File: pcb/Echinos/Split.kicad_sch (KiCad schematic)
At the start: 43 parts, among them J1 Conn_01x06_Socket, J2 Conn_01x06_Socket, J3 Conn_01x06_Socket, J5 Conn_01x05_Socket, J6 USB_B_Micro, J7 Conn_01x04_Socket, J8 USB_C_Receptacle_USB2.0, U2 USBLC6-2P6, U3 XC6210B332MR-G, U7 USBLC6-2P6, U8 74LVC1T45

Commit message: [PCB] - Save last state with on board RP2040.   - Create right side and route all components   - Component still on the bottom side to be able to merge both side for manufacturing
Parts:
- renumbered C3 to C222, C1 to C223, C2 to C224, D3 to D231, D1 to D232, F2 to F200, F3 to F201, FB1 to FB200, H1 to H200, H2 to H201, H5 to H202, H3 to H203, H4 to H204, H6 to H205, J6 to J200, J7 to J201, J4 to J202, J1 to J203, J2 to J204, J3 to J205, J8 to J206, J5 to J207, JP0 to JP200, JP13 to JP201, JP14 to JP202, JP15 to JP203, JP16 to JP204, JP11 to JP205, JP12 to JP206, JP205 to JP207, R13 to R206, R14 to R207, R15 to R208, R16 to R209, R7 to R210, R8 to R211, R9 to R212, R12 to R213, R1 to R214, U7 to U202, U8 to U203, U2 to U204, U3 to U205
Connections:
- net GND: now also J201.4 (Pin_4); no longer J201.1 (Pin_1)
- net P_RX: now also J201.3 (Pin_3); no longer J201.2 (Pin_2)
- net P_TX: now also J201.2 (Pin_2); no longer J201.3 (Pin_3)
- net VBUS_split: now also J201.1 (Pin_1); no longer J201.4 (Pin_4)
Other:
- sheet Backlight: file LED_left.kicad_sch -> LED.kicad_sch
- sheet Matrix: file Keyboard_Matrix.kicad_sch -> Matrix.kicad_sch
- title: Echinos -> Echinos Left
- moved on the sheet: C222, C223, C224, D231, D232, F200, F201, FB200, H200, H201, H202, H203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

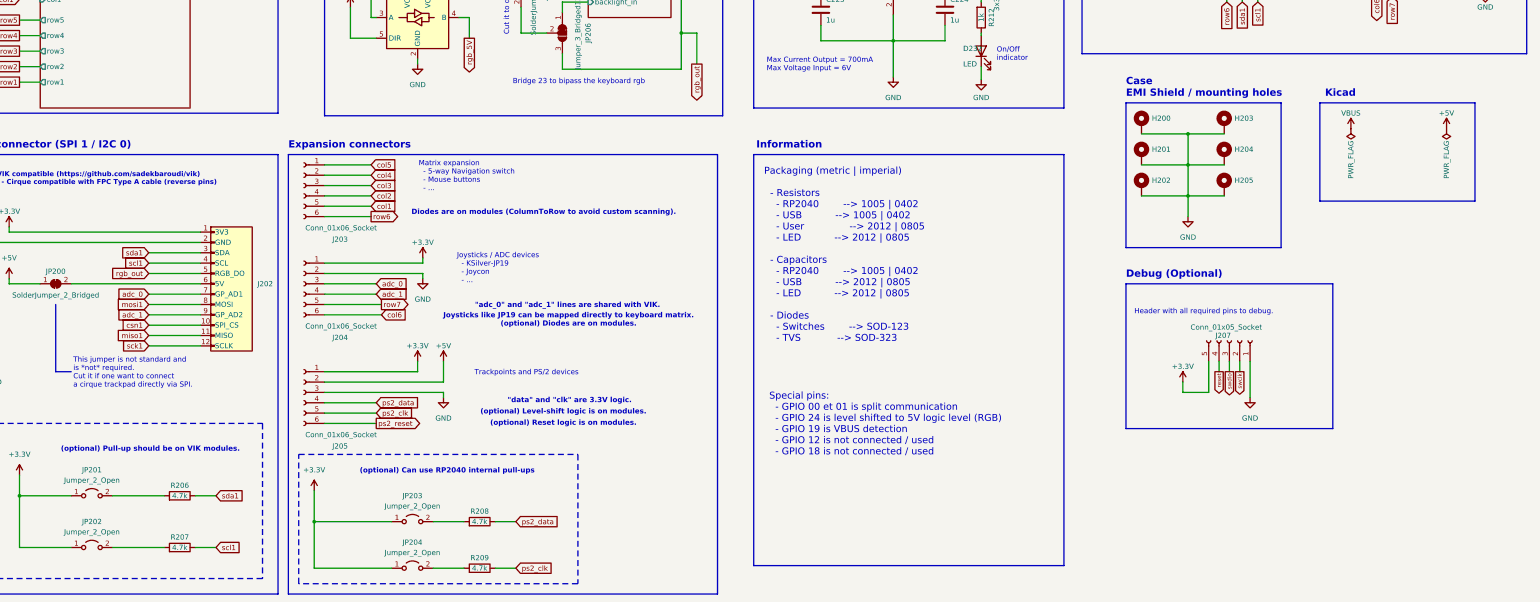
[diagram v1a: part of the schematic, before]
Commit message: [PCB] - Save last state with on board RP2040.   - Fix flash component orientation for JLCPCB assembly   - Add logo + version   - Add TH in flash footprint and use the same zone fill method as for RP2040 footprint   - Improve ground planes under switches (right side)   - Move unused schematics to backup folder (will be used to create keyboard modules later)   - Add manufacturer and part name (mfr)   - Mark optional parts as DNP   - Resync with official RP2040 symbol and update pins matching
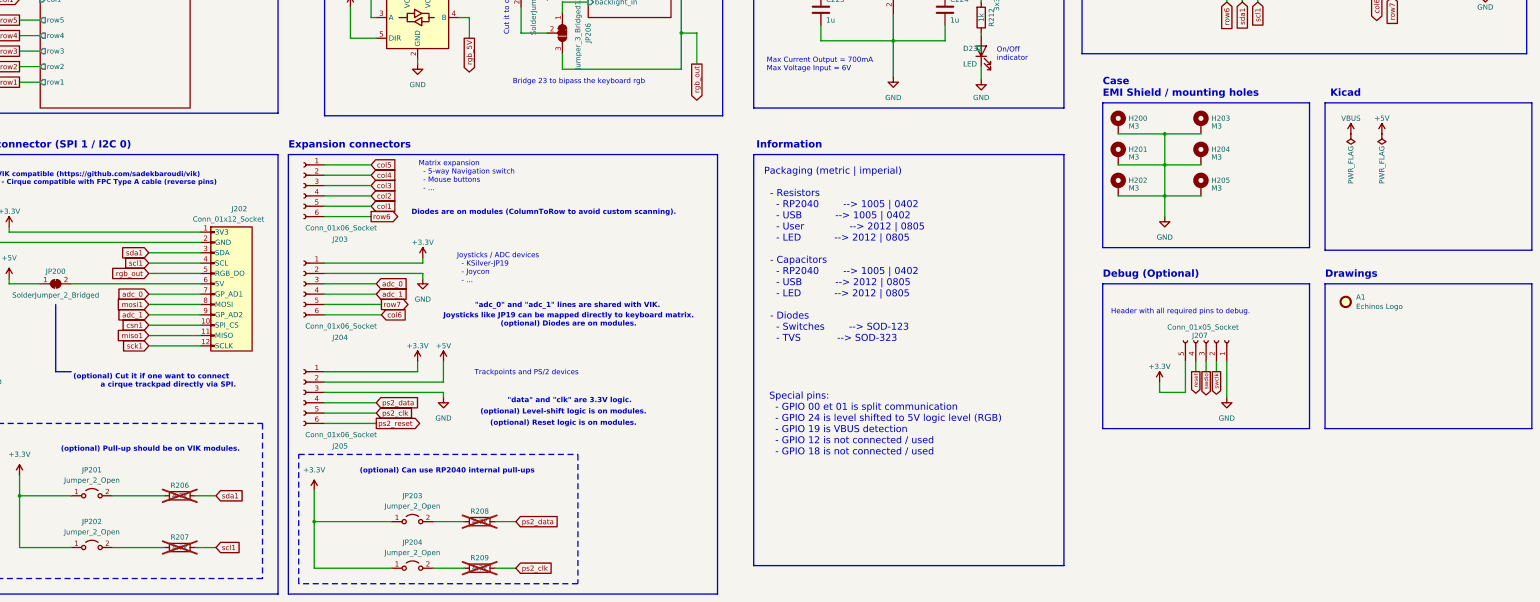
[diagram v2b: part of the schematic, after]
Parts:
- added A1: Echinos Logo, Echinos:Graphics_Hedgehog, symbol Mechanical:Fiducial
- C222: MFR (none) -> CL21B106KQQNNNE; Manufacturer (none) -> Samsung Electro-Mechanics
- C223, C224: MFR (none) -> CL21B105KOFNNNE; Manufacturer (none) -> Samsung Electro-Mechanics
- D231: MFR (none) -> B5817WS; Manufacturer (none) -> Shandong Jingdao Microelectronics
- D232: MFR (none) -> NCD0805G1; Manufacturer (none) -> Foshan NationStar Optoelectronics
- F200, F201: MFR (none) -> nSMD050; Manufacturer (none) -> TECHFUSE
- FB200: MFR (none) -> BLM21AG601SH1D; Manufacturer (none) -> Murata Electronics
- H200, H201, H202, H203, H204, H205: value MountHole -> M3
- J200: MFR (none) -> MICRO 4P DIP; Manufacturer (none) -> SHOU HAN
- J202: value ~ -> Conn_01x12_Socket; MFR (none) -> FPC05012-09200; Manufacturer (none) -> SHENZHEN ATOM TECH
- J203, J204, J205: MFR (none) -> 8.15A0.006200; Manufacturer (none) -> DIANWEI
- J206: MFR (none) -> USB4105-GF-A-060; Manufacturer (none) -> Global Connector Technology
- R206, R207, R208, R209: now not fitted
- R210, R211, R213: MFR (none) -> 0402WGF5101TCE; Manufacturer (none) -> UNI-ROYAL(Uniroyal Elec)
- R212: MFR (none) -> 0805W8F1001T5E; Manufacturer (none) -> UNI-ROYAL(Uniroyal Elec)
- R214: MFR (none) -> 0402WGF1002TCE; Manufacturer (none) -> UNI-ROYAL(Uniroyal Elec)
- U202, U204: MFR (none) -> USBLC6-2SC6; Manufacturer (none) -> TECH PUBLIC
- U203: MFR (none) -> SN74LVC1T45DBVR; Manufacturer (none) -> Texas Instruments
- U205: MFR (none) -> XC6210B332MR-G; Manufacturer (none) -> Torex Semicon
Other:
- note added: "(optional) Cut it if one want to connect a cirque trackpad directly via SPI."
- note added: "Drawings"
- note removed: "This jumper is not standard and is *not* required. Cut it if one want to connect a cirque trackpad directly via SPI."
- moved on the sheet: H200, H201, H202, H203, H204, H205, J207

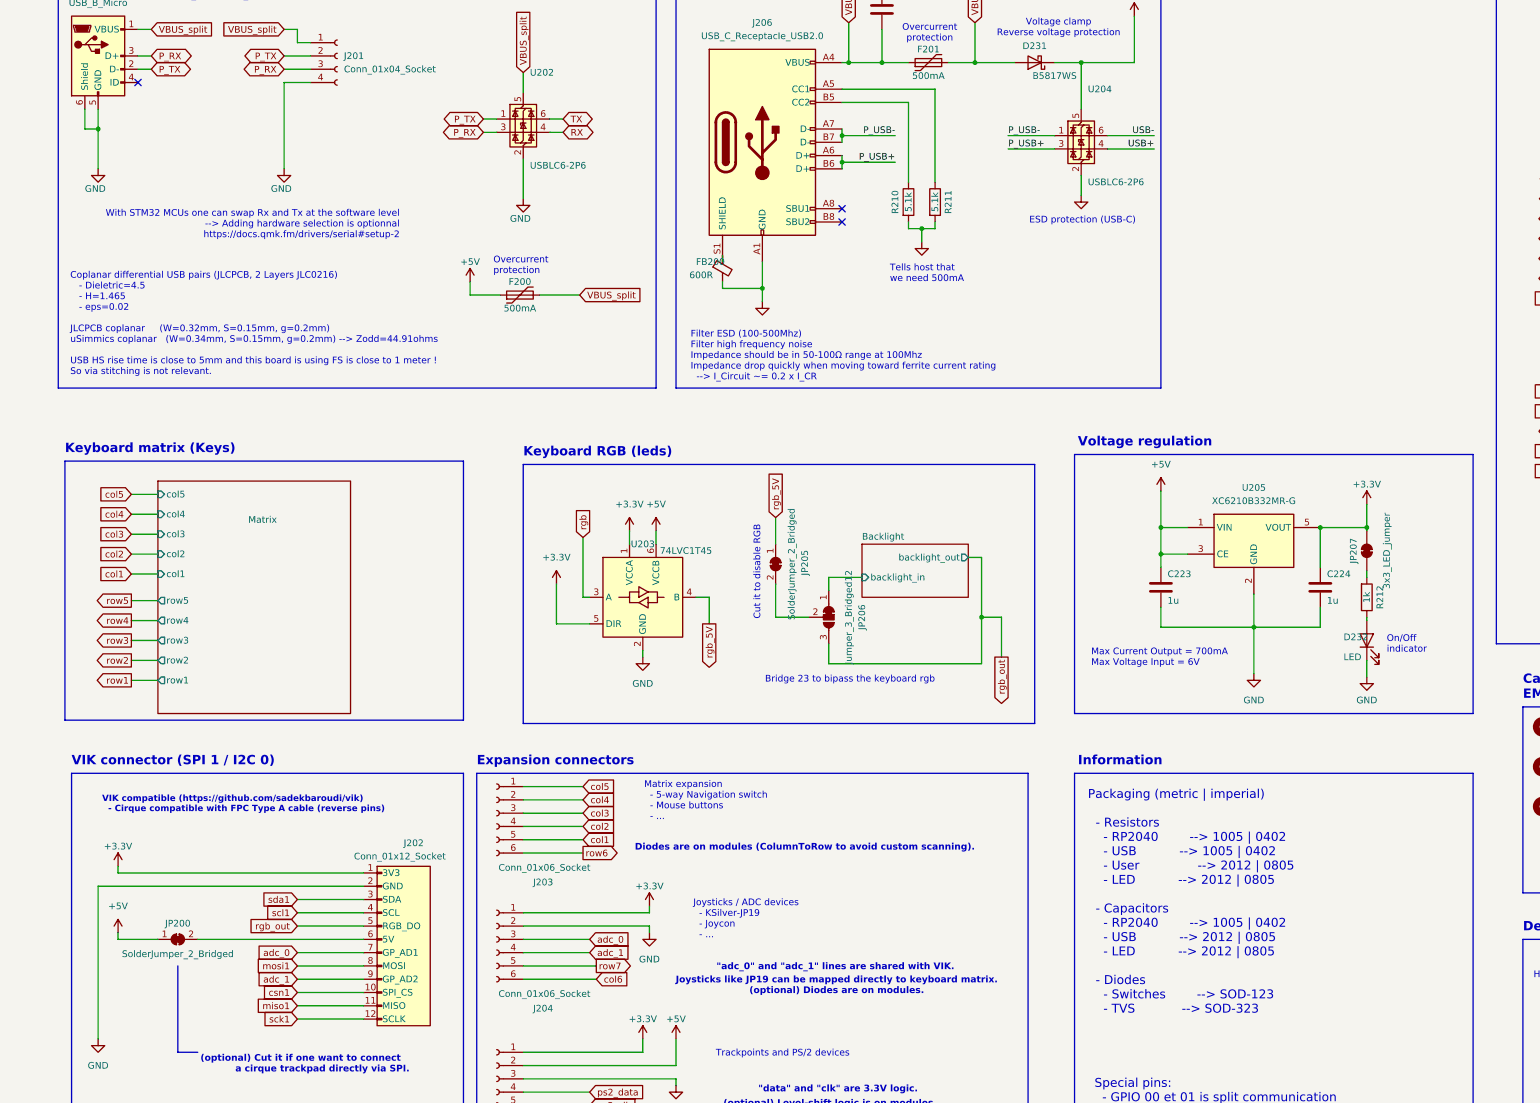
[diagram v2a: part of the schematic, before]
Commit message: [PCB] - Save last state with on board RP2040.   - Move to kicad 10   - Add DRC custom rule to exclude errors on PTH for switches due to holes being too close   - Move thermal via in both RP2040 and Flash memory to pad corners (better for manufacturing)   - Update USB footprint to match changes in kicad associated symbol   - Increase trackpoint holes from 3.0 to 3.2mm (cannot do more I guess)   - Removed unused footprint from library
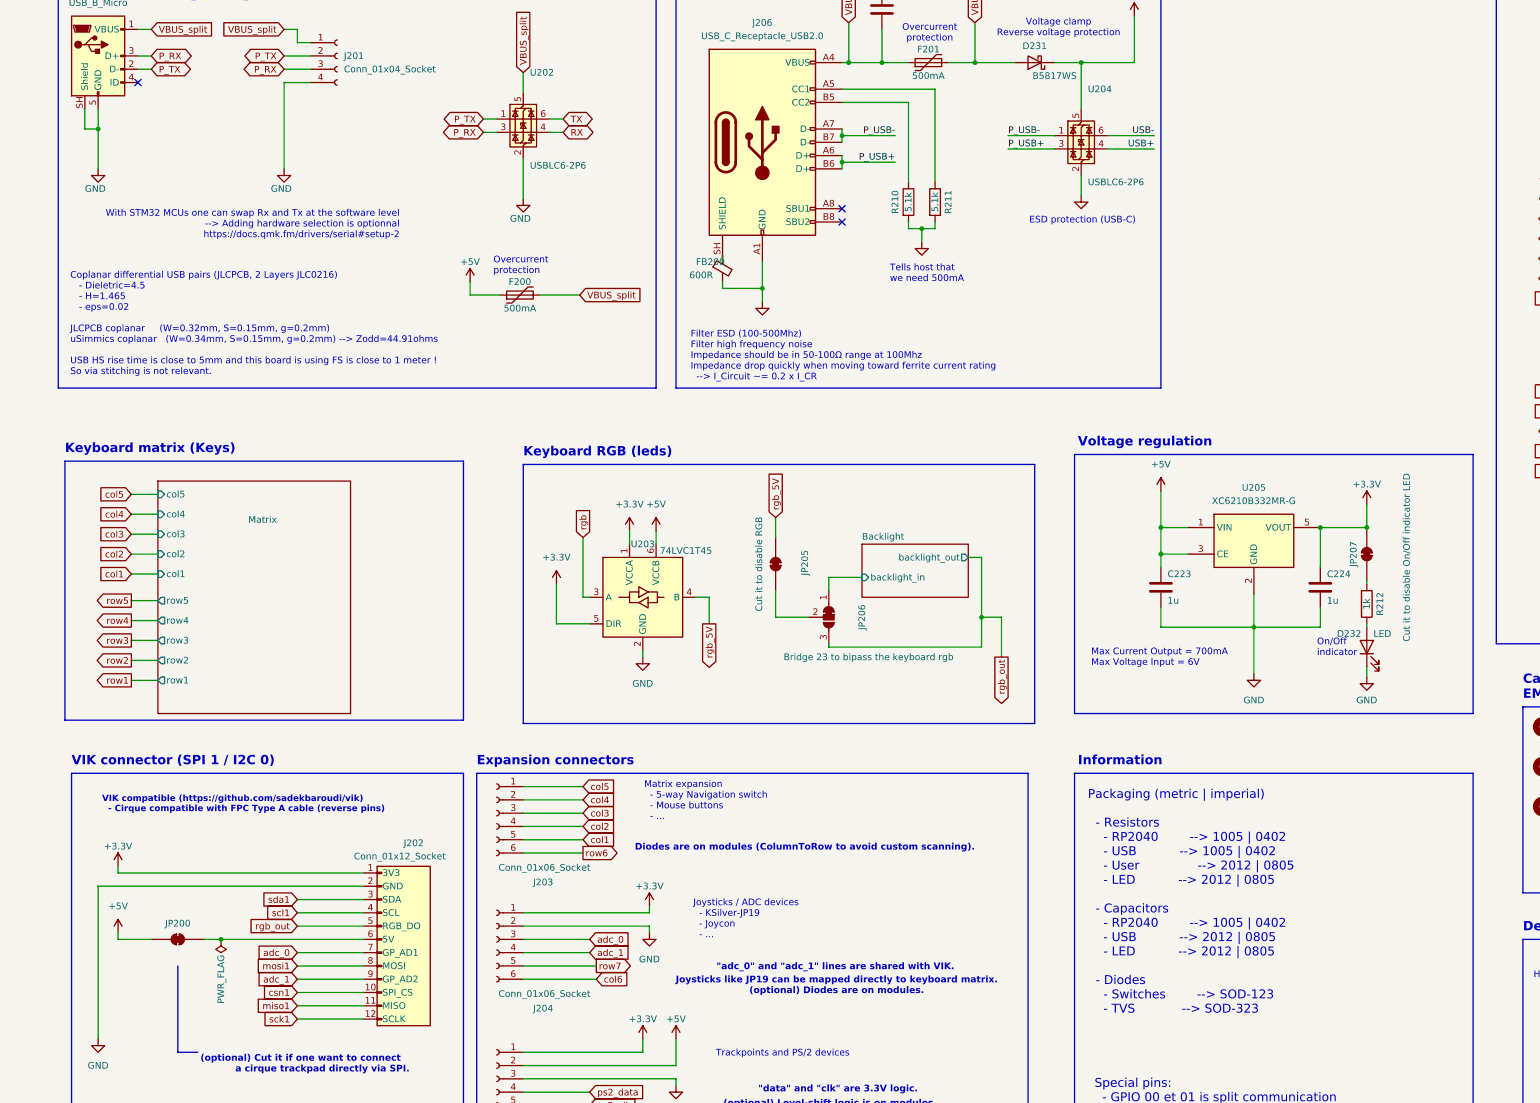
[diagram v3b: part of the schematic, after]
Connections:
- net GND: now also J200.SH (Shield); no longer J200.6 (Shield)
- net at FB200.1: now also J206.SH (SHIELD); no longer J206.S1 (SHIELD)
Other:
- note removed: "Bridge 23 to bipass the keyboard rgb"
- note removed: "Cut it to disable RGB"
- moved on the sheet: D232, JP207, R212

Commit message: 🚀 [PCB] - Board RP2040 sent in production.
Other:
- note added: "Case MX_C28T36"
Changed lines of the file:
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@@
+		)
+	)
+	(text "Case MX_C28T36"
+		(exclude_from_sim no)
+		(at 327.66 194.31 0)
+		(effects
+			(font
+				(size 1.5 1.5)
+				(thickness 0.3)
+				(bold yes)
+			)
+			(justify left bottom)
 		)
 	)
